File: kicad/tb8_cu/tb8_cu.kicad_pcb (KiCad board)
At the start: 4 copper layers, 219.4 x 85 mm, 45 parts, among them J1 Conn_02x25_Counter_Clockwise, U1 74AHCT74, U10 74AHCT193, U11 74AHCT193, U12 74AHCT193, U13 74AHCT193, U14 74AHCT573, U15 74AHCT573, U16 74HC00, U17 74HC00, U18 74HCT74, U19 74AHCT573, U2 74AHCT08, U20 74AHCT573, U21 74AHCT573, U22 74AHCT573, U3 74AHCT32, U4 74AHCT573, U5 74AHCT238, U6 74AHCT238, U7 74AHCT573, U8 74AHCT00, U9 74AHCT573

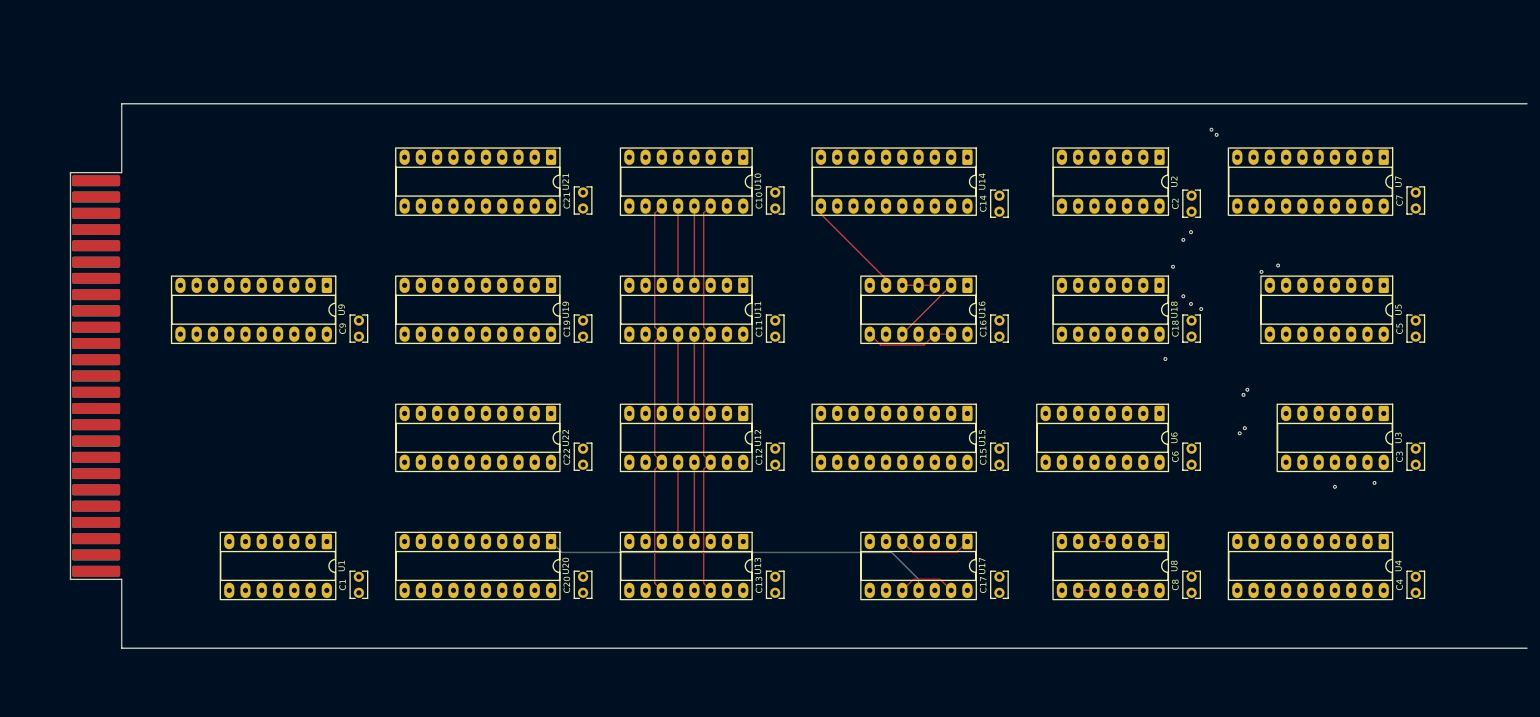
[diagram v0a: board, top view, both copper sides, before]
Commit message: tb8_cu first revision sch&pcb done
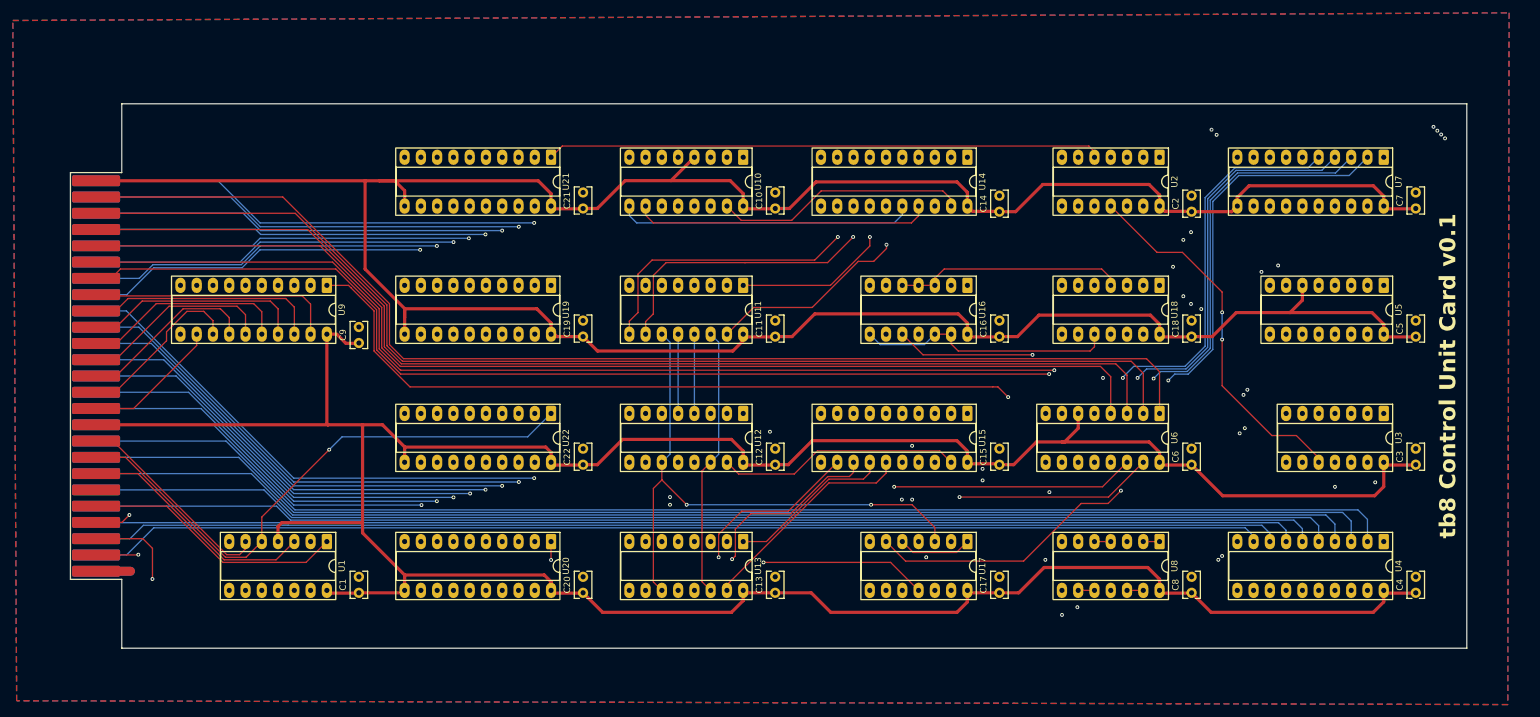
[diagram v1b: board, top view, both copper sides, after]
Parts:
- moved C9 1.00 mm to (69.0, 94.5)
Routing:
- net +5V: track 0.00 -> 937.6 mm
- net ta3: track 0.00 -> 347.4 mm, vias 0 -> 2
- net ta2: track 0.00 -> 346.4 mm, vias 0 -> 2
- net ta1: track 0.00 -> 345.5 mm, vias 0 -> 2
- net ta0: track 0.00 -> 344.5 mm, vias 0 -> 2
- net exc: track 20.3 -> 326.0 mm, vias 0 -> 4
- net t_wr: track 13.3 -> 267.2 mm, vias 0 -> 2
- net ldi: track 57.1 -> 291.3 mm
- net td0: track 109.2 -> 337.3 mm
- net ta4: track 71.8 -> 299.1 mm, vias 0 -> 2
- net ta5: track 71.8 -> 296.8 mm, vias 0 -> 2
- net td1: track 109.3 -> 333.4 mm
- net td2: track 109.2 -> 329.3 mm
- net eql: track 0.00 -> 219.4 mm, vias 0 -> 1
- net td3: track 109.2 -> 325.4 mm
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- added copper zone on B.Cu, net GND
- added copper zone on F.Cu, net GND
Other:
- board size 219.4 x 85 mm -> 210 x 85 mm
- board text added: "tb8 Control Unit Card v0.1"

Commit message: tb8_cu pcb routing cleanup
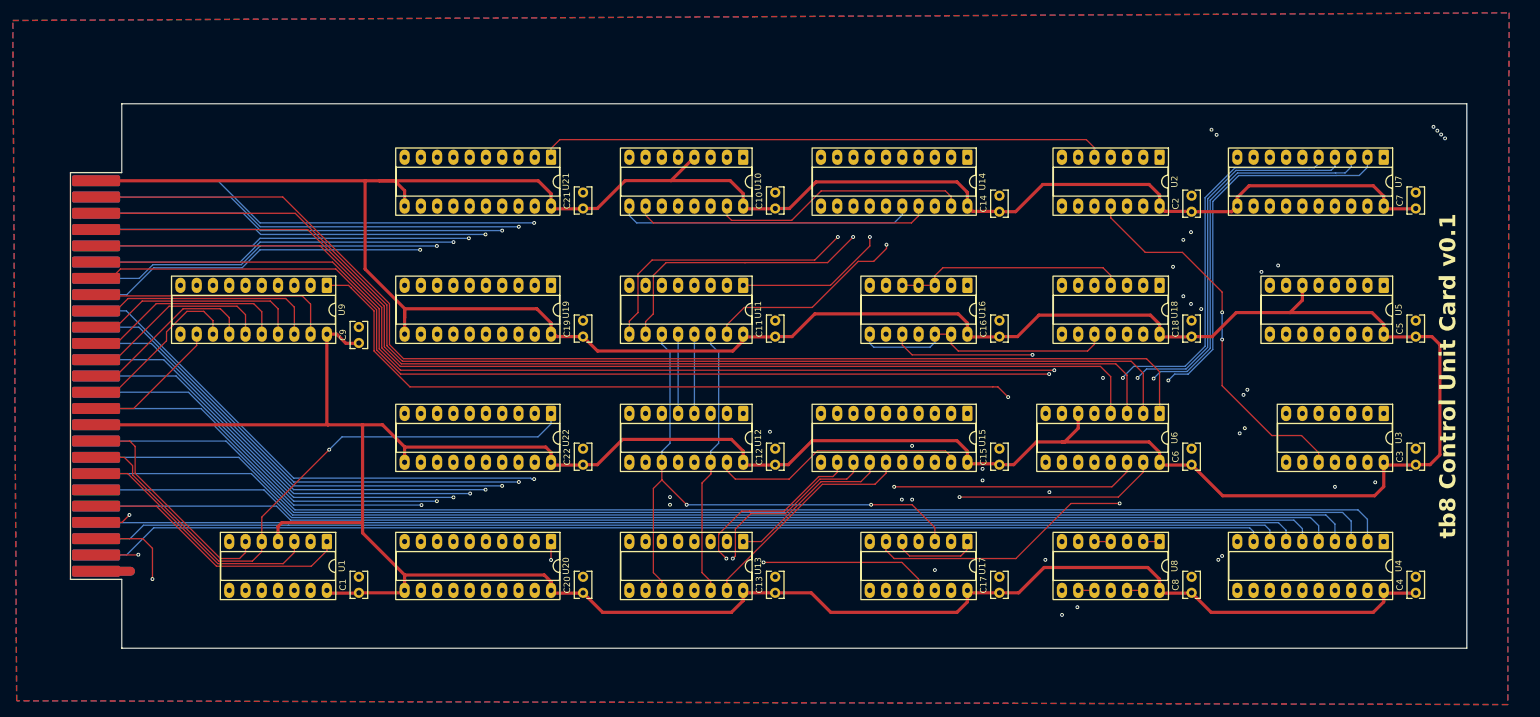
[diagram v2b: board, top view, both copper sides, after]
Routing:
- net +5V: track 937.6 -> 963.5 mm
- net exc: track 326.0 -> 334.3 mm
- net ldi: track 291.3 -> 298.9 mm
- net td7: track 307.1 -> 310.9 mm
- net td3: track 325.4 -> 329.2 mm
- net td4: track 321.8 -> 325.5 mm
- net td2: track 329.3 -> 333.0 mm
- net td5: track 317.6 -> 321.3 mm
- net td1: track 333.4 -> 337.0 mm
- net td6: track 314.7 -> 318.3 mm
- net t_wr: track 267.2 -> 270.5 mm
- net t_rd: track 253.9 -> 257.1 mm
- net td0: track 337.3 -> 340.4 mm
- net ta2: track 346.4 -> 349.5 mm
- net ta3: track 347.4 -> 350.3 mm
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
